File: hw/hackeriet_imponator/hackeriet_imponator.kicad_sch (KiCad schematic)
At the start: 0 parts

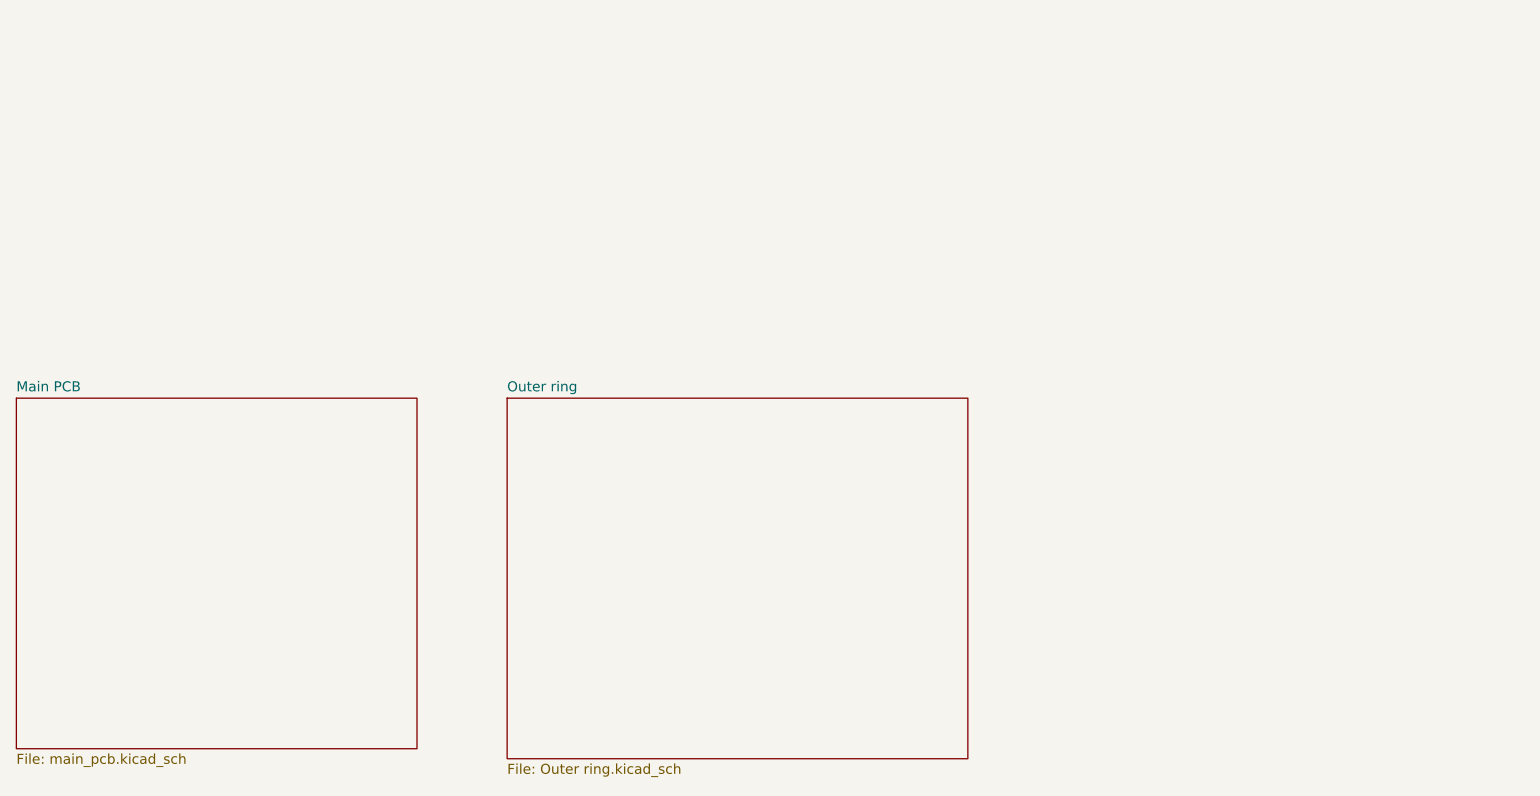
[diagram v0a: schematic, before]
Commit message: Major change. Resized PCB. Changed CPU. Added USB. Added headers. Added another layer for batteries
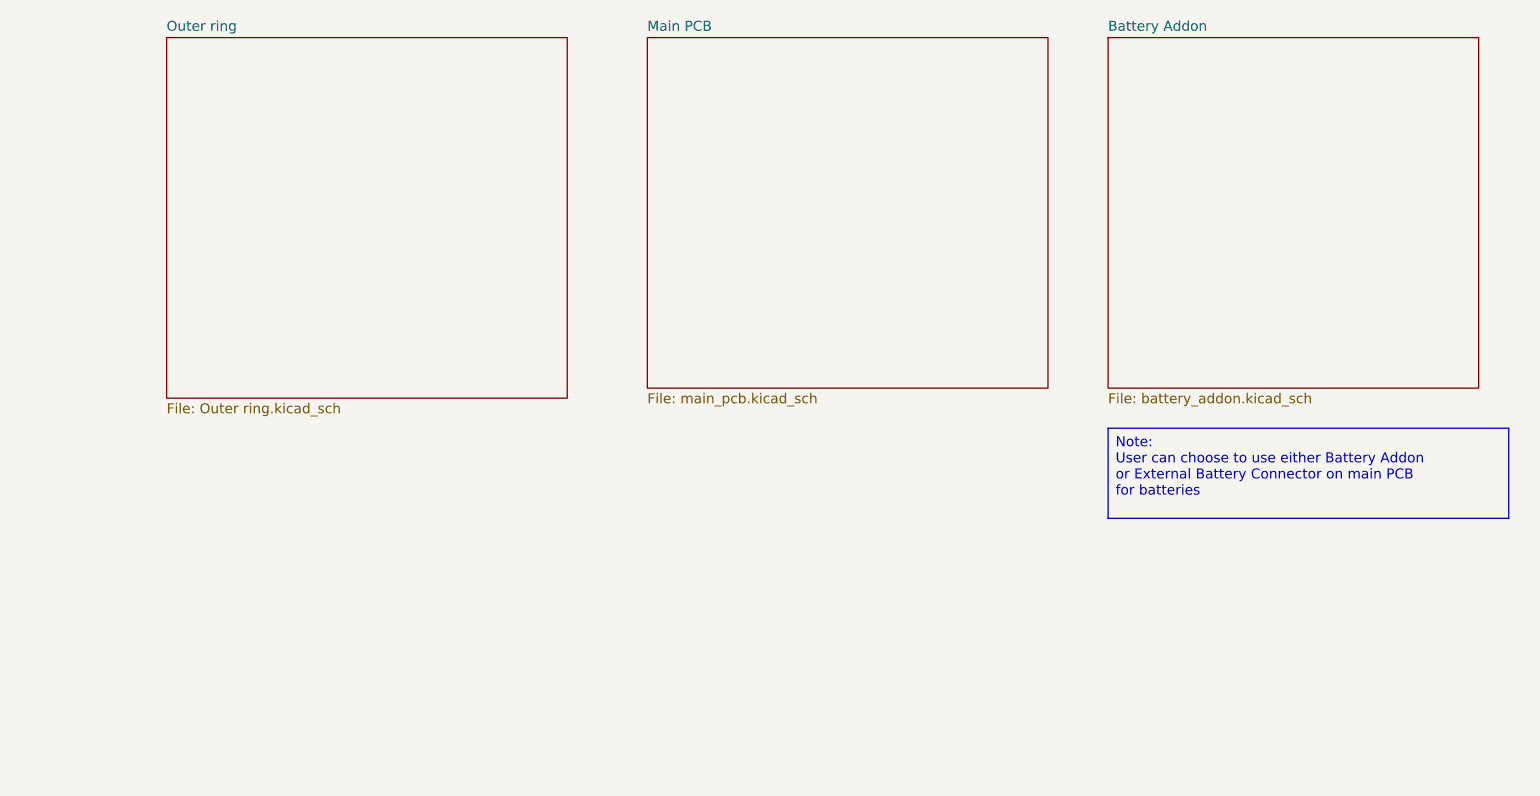
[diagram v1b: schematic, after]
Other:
- added sheet Battery Addon (battery_addon.kicad_sch)
- company: (none) -> Hackeriet
- title: (none) -> Imponator
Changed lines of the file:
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@@
 	(generator_version "9.0")
 	(paper "A4")
+	(title_block
+		(title "Imponator")
+		(date "2025-10-05")
+		(rev "1")
+		(company "Hackeriet")
+		(comment 1 "Designed by: Sigurd Hellesvik")
+	)
+	(text_box "Note:\nUser can choose to use either Battery Addon\nor External Battery Connector on main PCB\nfor batteries"
+		(exclude_from_sim no)
+		(at 165.1 132.08 0)
+		(size 50.8 11.43)
+		(margins 0.9525 0.9525 0.9525 0.9525)
+		(stroke
+			(width 0)
+			(type solid)
+		)
+		(fill
+			(type none)
+		)
+		(effects
+			(font
+				(size 1.27 1.27)
+			)
+			(justify left top)
+		)
+	)
 	(sheet
-		(at 26.67 128.27)
+		(at 106.68 82.55)
 		(size 50.8 44.45)
 		(exclude_from_sim no)
@@
 		)
 		(property "Sheetname" "Main PCB"
-			(at 26.67 127.5584 0)
+			(at 106.68 81.8384 0)
 			(effects
 				(font
@@
 		)
 		(property "Sheetfile" "main_pcb.kicad_sch"
-			(at 26.67 173.3046 0)
+			(at 106.68 127.5846 0)
 			(effects
 				(font
@@
 	)
 	(sheet
-		(at 88.9 128.27)
-		(size 58.42 45.72)
+		(at 165.1 82.55)
+		(size 46.99 44.45)
+		(exclude_from_sim no)
+		(in_bom yes)
+		(on_board yes)
+		(dnp no)
+		(fields_autoplaced yes)
+		(stroke
+			(width 0.1524)
+			(type solid)
+		)
+		(fill
+			(color 0 0 0 0.0000)
+		)
+		(property "Sheetname" "Battery Addon"
+			(at 165.1 81.8384 0)
+			(effects
+				(font
+					(size 1.27 1.27)
+				)
+				(justify left bottom)
+			)
+		)
+		(property "Sheetfile" "battery_addon.kicad_sch"
+			(at 165.1 127.5846 0)
+			(effects
+				(font
+					(size 1.27 1.27)
+				)
+				(justify left top)
+			)
+		)
+		(instances
+			(project "hackeriet_imponator"
+				(path "/469a2550-d397-4ef7-965d-96f8e6eb26aa"
+					(page "4")
+				)
+			)
+		)
+	)
+	(sheet
+		(at 45.72 82.55)
+		(size 50.8 45.72)
 		(exclude_from_sim no)
 		(in_bom yes)
@@
 		)
 		(property "Sheetname" "Outer ring"
-			(at 88.9 127.5584 0)
+			(at 45.72 81.8384 0)
 			(effects
 				(font
@@
 		)
 		(property "Sheetfile" "Outer ring.kicad_sch"
-			(at 88.9 174.5746 0)
+			(at 45.72 128.8546 0)
 			(effects
 				(font

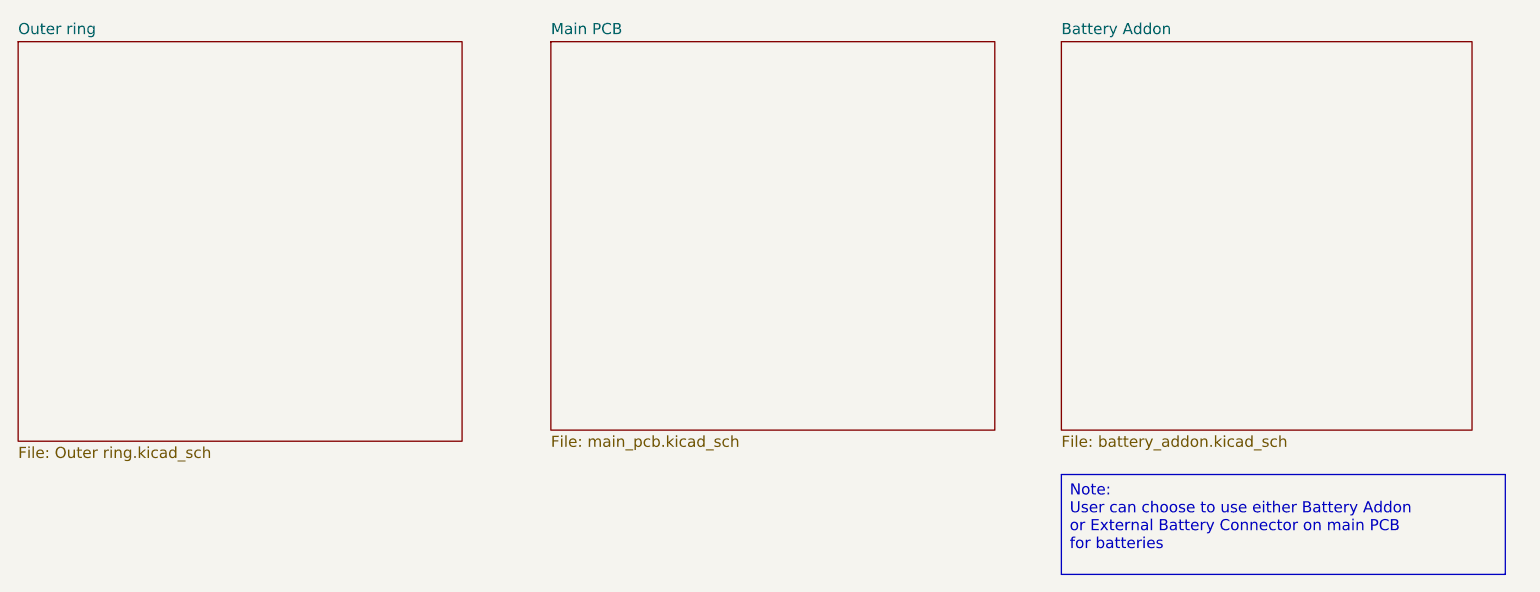
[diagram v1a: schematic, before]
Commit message: Removed outer ring and battery backplate. Ready to apply TODOs
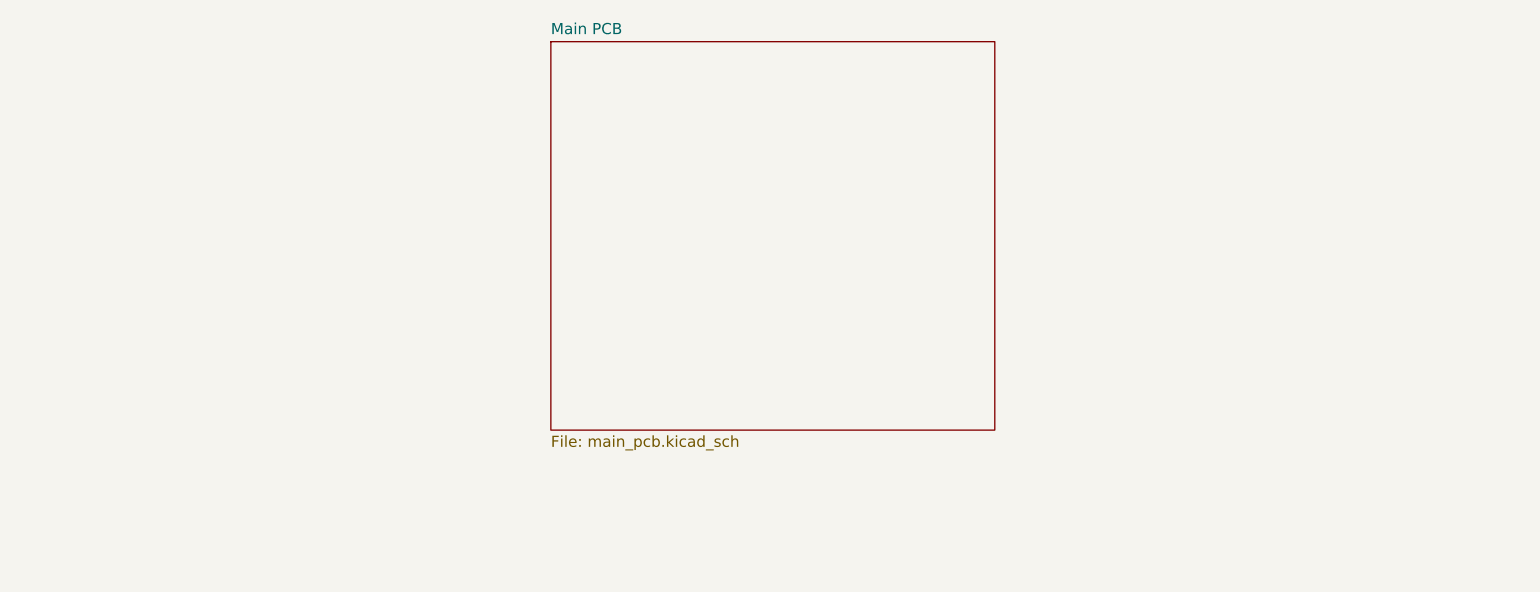
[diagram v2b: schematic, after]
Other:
- removed sheet Battery Addon
- removed sheet Outer ring
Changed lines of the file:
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@@
 		(comment 1 "Designed by: Sigurd Hellesvik")
-	)
-	(text_box "Note:\nUser can choose to use either Battery Addon\nor External Battery Connector on main PCB\nfor batteries"
-		(exclude_from_sim no)
-		(at 165.1 132.08 0)
-		(size 50.8 11.43)
-		(margins 0.9525 0.9525 0.9525 0.9525)
-		(stroke
-			(width 0)
-			(type solid)
-		)
-		(fill
-			(type none)
-		)
-		(effects
-			(font
-				(size 1.27 1.27)
-			)
-			(justify left top)
-		)
 	)
 	(sheet
@@
 				)
 			)
-		)
-	)
-	(sheet
-		(at 165.1 82.55)
-		(size 46.99 44.45)
-		(exclude_from_sim no)
-		(in_bom yes)
-		(on_board yes)
-		(dnp no)
-		(fields_autoplaced yes)
-		(stroke
-			(width 0.1524)
-			(type solid)
-		)
-		(fill
-			(color 0 0 0 0.0000)
-		)
-		(property "Sheetname" "Battery Addon"
-			(at 165.1 81.8384 0)
-			(effects
-				(font
-					(size 1.27 1.27)
-				)
-				(justify left bottom)
-			)
-		)
-		(property "Sheetfile" "battery_addon.kicad_sch"
-			(at 165.1 127.5846 0)
-			(effects
-				(font
-					(size 1.27 1.27)
-				)
-				(justify left top)
-			)
-		)
-		(instances
-			(project "hackeriet_imponator"
-				(path "/469a2550-d397-4ef7-965d-96f8e6eb26aa"
-					(page "4")
-				)
-			)
-		)
-	)
-	(sheet
-		(at 45.72 82.55)
-		(size 50.8 45.72)
-		(exclude_from_sim no)
-		(in_bom yes)
-		(on_board yes)
-		(dnp no)
-		(fields_autoplaced yes)
-		(stroke
-			(width 0.1524)
-			(type solid)
-		)
-		(fill
-			(color 0 0 0 0.0000)
-		)
-		(property "Sheetname" "Outer ring"
-			(at 45.72 81.8384 0)
-			(effects
-				(font
-					(size 1.27 1.27)
-				)
-				(justify left bottom)
-			)
-		)
-		(property "Sheetfile" "Outer ring.kicad_sch"
-			(at 45.72 128.8546 0)
-			(effects
-				(font
-					(size 1.27 1.27)
-				)
-				(justify left top)
-			)
-		)
-		(instances
-			(project "hackeriet_imponator"
-				(path "/469a2550-d397-4ef7-965d-96f8e6eb26aa"
-					(page "3")
-				)
-			)

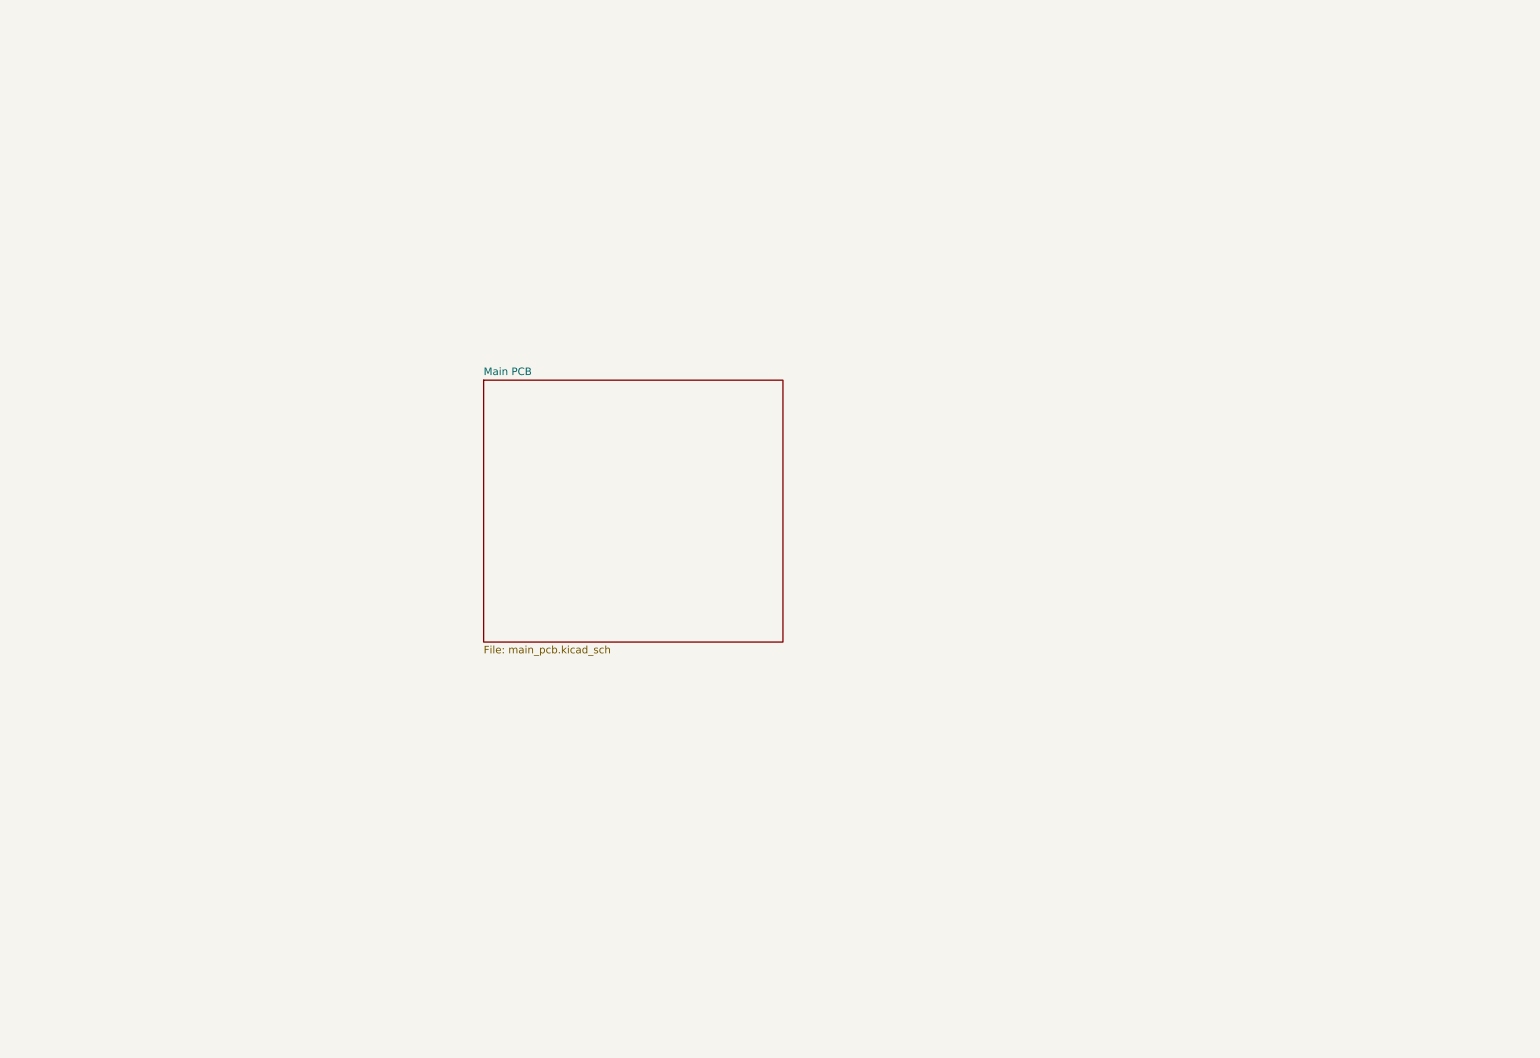
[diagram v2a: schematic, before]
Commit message: Added switch between batt and USB. Changed LEDs to sideways
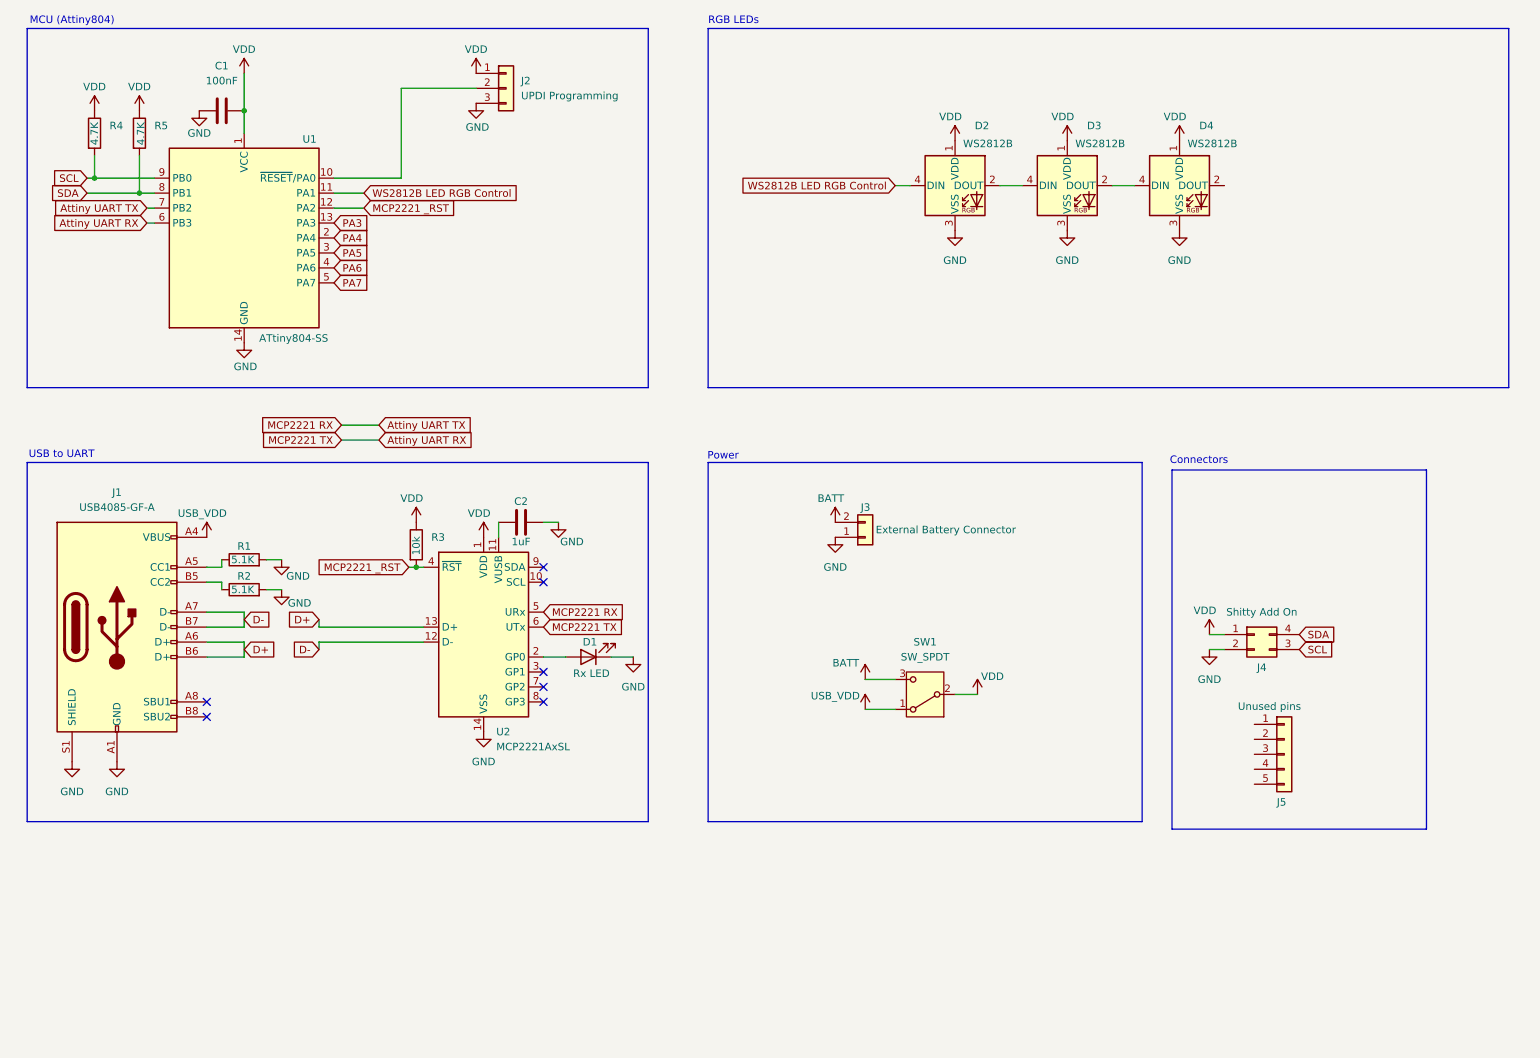
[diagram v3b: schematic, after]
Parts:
- added C1: 100nF, Capacitor_SMD:C_0603_1608Metric_Pad1.08x0.95mm_HandSolder, symbol Device:C
- added C2: 1uF, Capacitor_SMD:C_0603_1608Metric_Pad1.08x0.95mm_HandSolder, symbol Device:C
- added D1: Rx LED, LED_SMD:LED_0603_1608Metric_Pad1.05x0.95mm_HandSolder, symbol Device:LED
- added D2, D3, D4: WS2812B, imponator_footprint_lib:LED_WS2812B-4020, symbol LED:WS2812B
- added J1: USB4085-GF-A, Connector_USB:USB_C_Receptacle_GCT_USB4085, symbol Connector:USB_C_Receptacle_USB2.0_16P
- added J2: UPDI Programming, Connector_PinHeader_2.54mm:PinHeader_1x03_P2.54mm_Horizontal, symbol Connector_Generic:Conn_01x03
- added J3: External Battery Connector, Connector_PinHeader_2.54mm:PinHeader_1x02_P2.54mm_Vertical, symbol Connector_Generic:Conn_01x02
- added J4: Shitty Add On, Connector_PinHeader_2.54mm:PinHeader_2x02_P2.54mm_Horizontal, symbol Connector_Generic:Conn_02x02_Counter_Clockwise
- added J5: Unused pins, Connector_PinSocket_2.54mm:PinSocket_1x05_P2.54mm_Vertical_SMD_Pin1Left, symbol Connector_Generic:Conn_01x05
- added R1, R2: 5.1K, Resistor_SMD:R_0603_1608Metric_Pad0.98x0.95mm_HandSolder, symbol Device:R
- added R3: 10k, Resistor_SMD:R_0603_1608Metric_Pad0.98x0.95mm_HandSolder, symbol Device:R
- added R4, R5: 4.7K, Resistor_SMD:R_0603_1608Metric_Pad0.98x0.95mm_HandSolder, symbol Device:R
- added SW1: SW_SPDT, Button_Switch_SMD:SW_SPDT_Shouhan_MSK12C02, symbol Switch:SW_SPDT
- added U1: ATtiny804-SS, Package_SO:SOIC-14_3.9x8.7mm_P1.27mm, symbol MCU_Microchip_ATtiny:ATtiny804-SS
- added U2: MCP2221AxSL, Package_SO:SOIC-14_3.9x8.7mm_P1.27mm, symbol Interface_USB:MCP2221AxSL
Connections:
- new net: D2.2 (DOUT), D3.4 (DIN)
- new net: D3.2 (DOUT), D4.4 (DIN)
- new net: J1.A5 (CC1), R1.1
- new net: C2.1, U2.11 (VUSB)
- new net: J1.B5 (CC2), R2.1
- new net: J2.2 (Pin_2), U1.10 (~{RESET}/PA0)
- new net: D1.2 (A), U2.2 (GP0)
- new net Attiny UART RX: U1.6 (PB3), U2.6 (UTx)
- new net Attiny UART TX: U1.7 (PB2), U2.5 (URx)
- new net BATT: J3.2 (Pin_2), SW1.3 (C)
- new net D+: J1.A6 (D+), J1.B6 (D+), U2.13 (D+)
- new net D-: J1.A7 (D-), J1.B7 (D-), U2.12 (D-)
- new net GND: C1.1, C2.2, D1.1 (K), D2.3 (VSS), D3.3 (VSS), D4.3 (VSS), J1.A1 (GND), J1.A12 (GND), J1.B1 (GND), J1.B12 (GND), J1.S1 (SHIELD), J2.3 (Pin_3), J3.1 (Pin_1), J4.2 (Pin_2), R1.2, R2.2, U1.14 (GND), U2.14 (VSS)
- new net MCP2221 _RST: R3.2, U1.12 (PA2), U2.4 (~{RST})
- new net PA3: U1.13 (PA3)
- new net PA4: U1.2 (PA4)
- new net PA5: U1.3 (PA5)
- new net PA6: U1.4 (PA6)
- new net PA7: U1.5 (PA7)
- new net SCL: J4.3 (Pin_3), R4.2, U1.9 (PB0)
- new net SDA: J4.4 (Pin_4), R5.2, U1.8 (PB1)
- new net USB_VDD: J1.A4 (VBUS), J1.A9 (VBUS), J1.B4 (VBUS), J1.B9 (VBUS), SW1.1 (A)
- new net VDD: C1.2, D2.1 (VDD), D3.1 (VDD), D4.1 (VDD), J2.1 (Pin_1), J4.1 (Pin_1), R3.1, R4.1, R5.1, SW1.2 (B), U1.1 (VCC), U2.1 (VDD)
- new net WS2812B LED RGB Control: D2.4 (DIN), U1.11 (PA1)
- no-connect marks 0 -> 7
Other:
- removed sheet Main PCB
- note added: "Connectors"
- note added: "MCU (Attiny804)"
- note added: "Power"
- note added: "RGB LEDs"
- note added: "USB to UART"
